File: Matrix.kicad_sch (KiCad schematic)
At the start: 56 parts

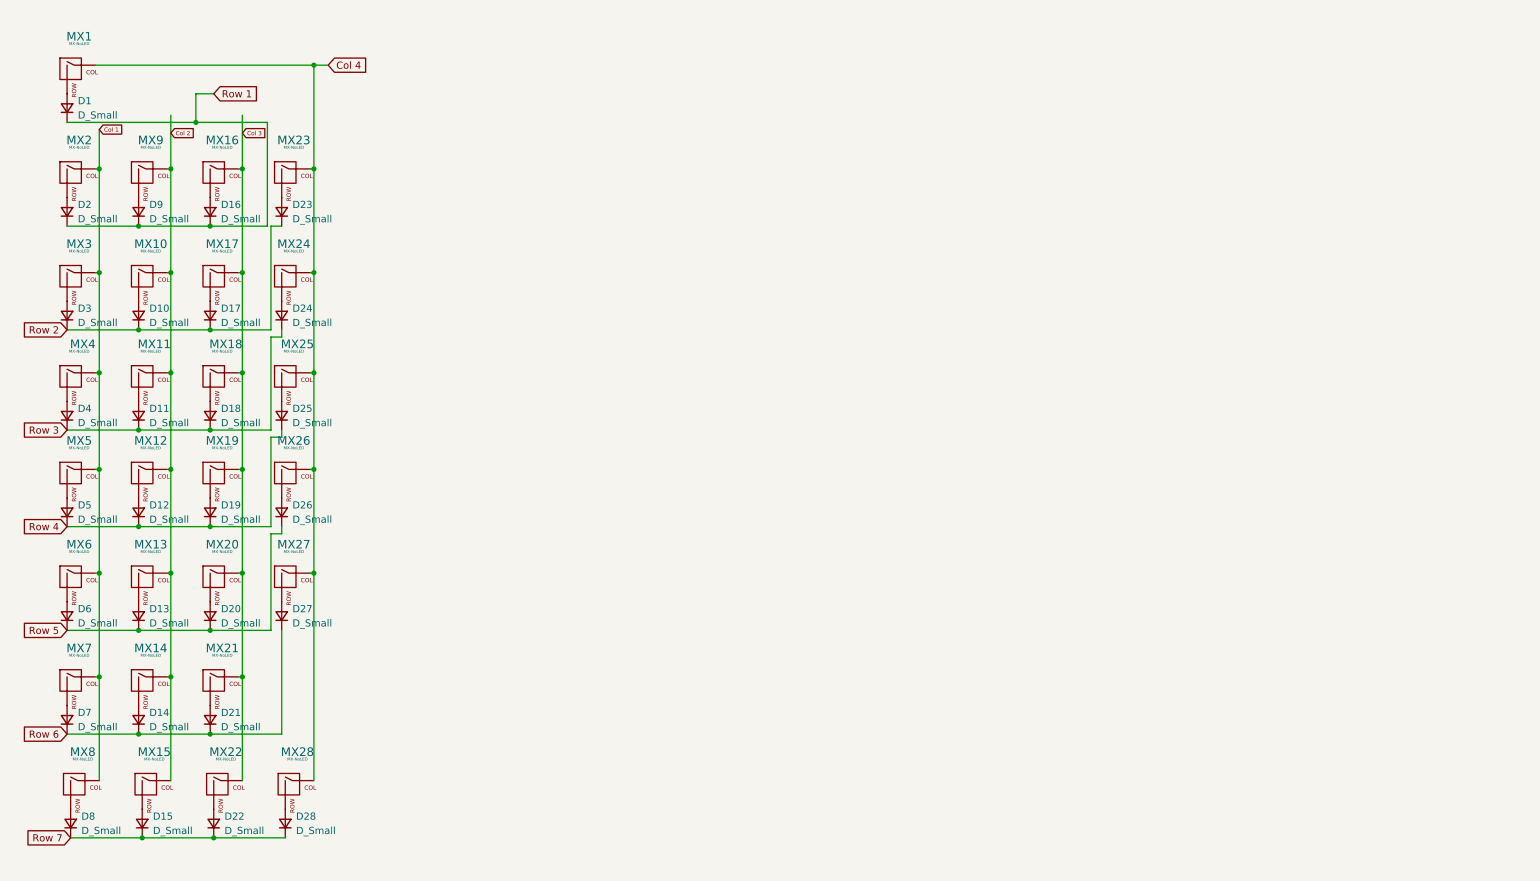
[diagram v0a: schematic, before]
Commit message: Schematic Finallized
Added ESD Protection to USB input and RGB LEDs
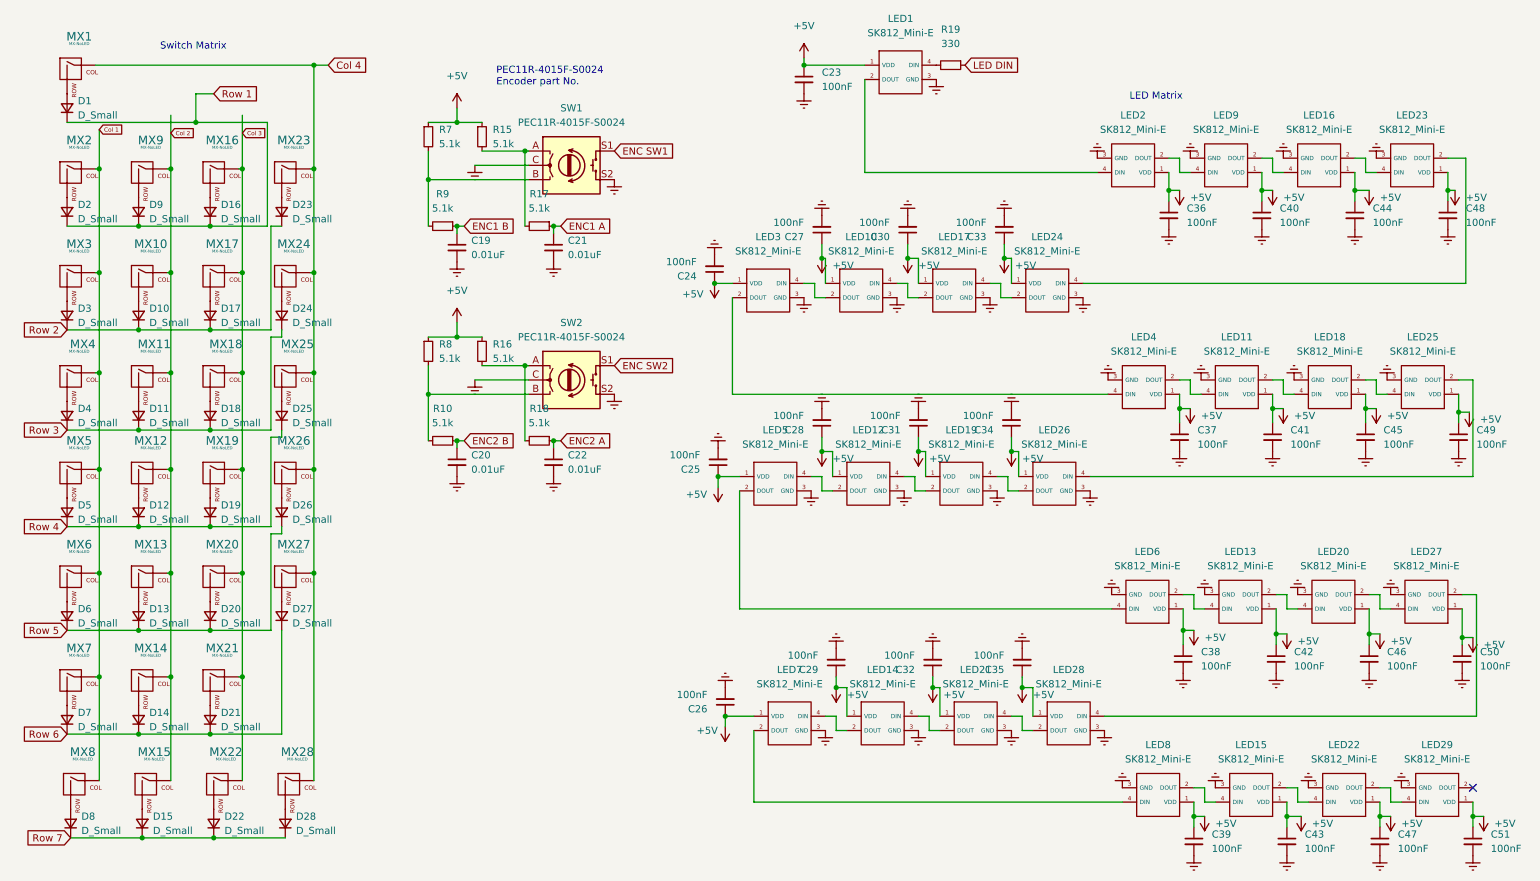
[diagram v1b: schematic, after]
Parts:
- added C19, C20, C21, C22: 0.01uF, Capacitor_SMD:C_0603_1608Metric_Pad1.08x0.95mm_HandSolder, symbol Device:C_Small
- added C23, C24, C25, C26, C27, C28, C29, C30, C31, C32, C33, C34, C35, C36, C37, C38, C39, C40, C41, C42, C43, C44, C45, C46, C47, C48, C49, C50, C51: 100nF, Capacitor_SMD:C_0603_1608Metric_Pad1.08x0.95mm_HandSolder, symbol Device:C_Small
- added LED1, LED10, LED11, LED12, LED13, LED14, LED15, LED16, LED17, LED18, LED19, LED2, LED20, LED21, LED22, LED23, LED24, LED25, LED26, LED27, LED28, LED29, LED3, LED4, LED5, LED6, LED7, LED8, LED9: SK812_Mini-E, Reset Switch:SK812 Mini-E, symbol Reset Switch:SK812_Mini-E
- added R10, R15, R16, R17, R18, R7, R8, R9: 5.1k, Resistor_SMD:R_0603_1608Metric_Pad0.98x0.95mm_HandSolder, symbol Device:R_Small
- added R19: 330, Resistor_SMD:R_0603_1608Metric_Pad0.98x0.95mm_HandSolder, symbol Device:R_Small
- added SW1, SW2: PEC11R-4015F-S0024, Reset Switch:PEC11R-4015F-S0024, symbol Reset Switch:PEC11R-4015F-S0024
- D1, D10, D11, D12, D13, D14, D15, D16, D17, D18, D19, D2, D20, D21, D22, D23, D24, D25, D26, D27, D28, D3, D4, D5, D6, D7, D8, D9: footprint (none) -> Diode_SMD:D_SOD-523
- MX1, MX10, MX11, MX12, MX13, MX14, MX15, MX16, MX17, MX18, MX19, MX2, MX20, MX21, MX22, MX23, MX24, MX25, MX26, MX27, MX3, MX4, MX5, MX6, MX7, MX8, MX9: footprint (none) -> MX_Only:MXOnly-1U-Hotswap
- MX28: footprint (none) -> MX_Only:MXOnly-2U-Hotswap-VerticalStabilizers
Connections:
- new net: R7.2, R9.2, SW1.B
- new net: LED18.2 (DOUT), LED25.4 (DIN)
- new net: LED11.2 (DOUT), LED18.4 (DIN)
- new net: LED22.2 (DOUT), LED29.4 (DIN)
- new net: R16.2, R18.2, SW2.A
- new net: R10.2, R8.2, SW2.B
- new net: LED27.2 (DOUT), LED28.4 (DIN)
- new net: LED20.2 (DOUT), LED27.4 (DIN)
- new net: LED14.4 (DIN), LED21.2 (DOUT)
- new net: LED21.4 (DIN), LED28.2 (DOUT)
- new net: LED13.2 (DOUT), LED20.4 (DIN)
- new net: LED13.4 (DIN), LED6.2 (DOUT)
- new net: LED25.2 (DOUT), LED26.4 (DIN)
- new net: LED5.2 (DOUT), LED6.4 (DIN)
- new net: LED16.2 (DOUT), LED23.4 (DIN)
- new net: LED16.4 (DIN), LED9.2 (DOUT)
- new net: R15.2, R17.2, SW1.A
- new net: LED1.4 (DIN), R19.2
- new net: LED10.2 (DOUT), LED3.4 (DIN)
- new net: LED10.4 (DIN), LED17.2 (DOUT)
- new net: LED19.4 (DIN), LED26.2 (DOUT)
- new net: LED23.2 (DOUT), LED24.4 (DIN)
- new net: LED12.2 (DOUT), LED5.4 (DIN)
- new net: LED12.4 (DIN), LED19.2 (DOUT)
- new net: LED17.4 (DIN), LED24.2 (DOUT)
- new net: LED3.2 (DOUT), LED4.4 (DIN)
- new net: LED15.2 (DOUT), LED22.4 (DIN)
- new net: LED15.4 (DIN), LED8.2 (DOUT)
- new net: LED7.2 (DOUT), LED8.4 (DIN)
- new net: LED14.2 (DOUT), LED7.4 (DIN)
- new net: LED2.2 (DOUT), LED9.4 (DIN)
- new net: LED1.2 (DOUT), LED2.4 (DIN)
- new net: LED11.4 (DIN), LED4.2 (DOUT)
- new net +5V: C23.1, C24.1, C25.1, C26.1, C27.1, C28.1, C29.1, C30.1, C31.1, C32.1, C33.1, C34.1, C35.1, C36.1, C37.1, C38.1, C39.1, C40.1, C41.1, C42.1, C43.1, C44.1, C45.1, C46.1, C47.1, C48.1, C49.1, C50.1, C51.1, LED1.1 (VDD), LED10.1 (VDD), LED11.1 (VDD), LED12.1 (VDD), LED13.1 (VDD), LED14.1 (VDD), LED15.1 (VDD), LED16.1 (VDD), LED17.1 (VDD), LED18.1 (VDD), LED19.1 (VDD), LED2.1 (VDD), LED20.1 (VDD), LED21.1 (VDD), LED22.1 (VDD), LED23.1 (VDD), LED24.1 (VDD), LED25.1 (VDD), LED26.1 (VDD), LED27.1 (VDD), LED28.1 (VDD), LED29.1 (VDD), LED3.1 (VDD), LED4.1 (VDD), LED5.1 (VDD), LED6.1 (VDD), LED7.1 (VDD), LED8.1 (VDD), LED9.1 (VDD), R15.1, R16.1, R7.1, R8.1
- new net ENC SW1: SW1.S1
- new net ENC SW2: SW2.S1
- new net ENC1 A: C21.1, R17.1
- new net ENC1 B: C19.1, R9.1
- new net ENC2 A: C22.1, R18.1
- new net ENC2 B: C20.1, R10.1
- new net Earth: C19.2, C20.2, C21.2, C22.2, C23.2, C24.2, C25.2, C26.2, C27.2, C28.2, C29.2, C30.2, C31.2, C32.2, C33.2, C34.2, C35.2, C36.2, C37.2, C38.2, C39.2, C40.2, C41.2, C42.2, C43.2, C44.2, C45.2, C46.2, C47.2, C48.2, C49.2, C50.2, C51.2, LED1.3 (GND), LED10.3 (GND), LED11.3 (GND), LED12.3 (GND), LED13.3 (GND), LED14.3 (GND), LED15.3 (GND), LED16.3 (GND), LED17.3 (GND), LED18.3 (GND), LED19.3 (GND), LED2.3 (GND), LED20.3 (GND), LED21.3 (GND), LED22.3 (GND), LED23.3 (GND), LED24.3 (GND), LED25.3 (GND), LED26.3 (GND), LED27.3 (GND), LED28.3 (GND), LED29.3 (GND), LED3.3 (GND), LED4.3 (GND), LED5.3 (GND), LED6.3 (GND), LED7.3 (GND), LED8.3 (GND), LED9.3 (GND), SW1.C, SW1.S2, SW2.C, SW2.S2
- new net LED DIN: R19.1
- no-connect marks 0 -> 1
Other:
- note added: "LED Matrix"
- note added: "PEC11R-4015F-S0024 Encoder part No."
- note added: "Switch Matrix"

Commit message: Layout Roughed in, routing started
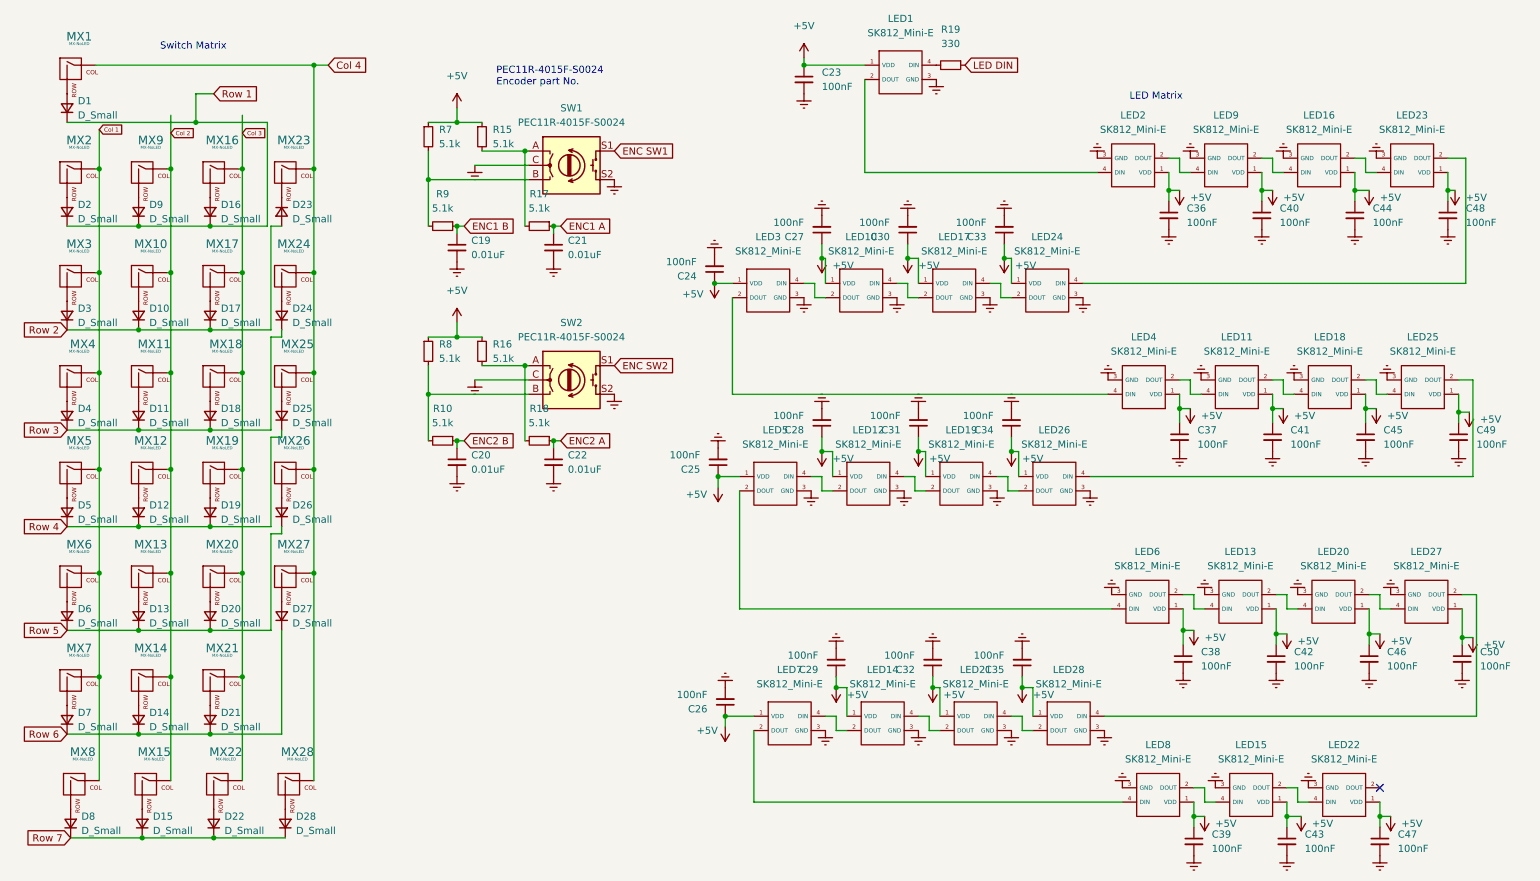
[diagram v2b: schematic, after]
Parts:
- removed C51: 100nF, Capacitor_SMD:C_0603_1608Metric_Pad1.08x0.95mm_HandSolder, symbol Device:C_Small
- removed LED29: SK812_Mini-E, Reset Switch:SK812 Mini-E, symbol Reset Switch:SK812_Mini-E
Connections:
- net Row 2: now also D23.2 (A); no longer D23.1 (K)
- net at MX23.2 (ROW): now also D23.1 (K); no longer D23.2 (A)
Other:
- moved on the sheet: D23
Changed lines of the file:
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@@
   (junction (at 68.58 76.2) (diameter 0) (color 0 0 0 0)
   )
-  (junction (at 274.32 154.94) (diameter 0) (color 0 0 0 0)
-  )
   (junction (at 50.165 68.58) (diameter 0) (color 0 0 0 0)
   )
@@
   (junction (at 55.88 111.76) (diameter 0) (color 0 0 0 0)
   )
-  (no_connect (at 274.32 149.86))
+  (no_connect (at 257.81 149.86))
   (wire (pts (xy 158.75 53.34) (xy 158.75 55.88))
     (stroke (width 0) (type default) (color 0 0 0 0))
@@
     (stroke (width 0) (type default) (color 0 0 0 0))
   )
-  (wire (pts (xy 257.81 149.86) (xy 259.715 149.86))
-    (stroke (width 0) (type default) (color 0 0 0 0))
-  )
   (wire (pts (xy 224.79 152.4) (xy 224.79 154.94))
     (stroke (width 0) (type default) (color 0 0 0 0))
@@
     (stroke (width 0) (type default) (color 0 0 0 0))
   )
-  (wire (pts (xy 259.715 149.86) (xy 259.715 152.4))
-    (stroke (width 0) (type default) (color 0 0 0 0))
-  )
   (wire (pts (xy 37.465 121.92) (xy 50.165 121.92))
     (stroke (width 0) (type default) (color 0 0 0 0))
@@
     (stroke (width 0) (type default) (color 0 0 0 0))
   )
+  (wire (pts (xy 60.325 31.75) (xy 60.325 50.165))
+    (stroke (width 0) (type default) (color 0 0 0 0))
+  )
   (wire (pts (xy 60.96 103.505) (xy 60.96 87.63))
     (stroke (width 0) (type default) (color 0 0 0 0))
@@
     (stroke (width 0) (type default) (color 0 0 0 0))
   )
-  (wire (pts (xy 274.32 154.94) (xy 274.32 156.845))
-    (stroke (width 0) (type default) (color 0 0 0 0))
-  )
-  (wire (pts (xy 60.325 50.165) (xy 60.325 31.75))
-    (stroke (width 0) (type default) (color 0 0 0 0))
-  )
   (wire (pts (xy 50.8 158.75) (xy 63.5 158.75))
     (stroke (width 0) (type default) (color 0 0 0 0))
@@
     (stroke (width 0) (type default) (color 0 0 0 0))
   )
-  (wire (pts (xy 259.715 152.4) (xy 261.62 152.4))
-    (stroke (width 0) (type default) (color 0 0 0 0))
-  )
   (wire (pts (xy 255.27 82.55) (xy 255.27 85.09))
     (stroke (width 0) (type default) (color 0 0 0 0))
@@
     (stroke (width 0) (type default) (color 0 0 0 0))
   )
-  (wire (pts (xy 274.32 154.94) (xy 276.225 154.94))
-    (stroke (width 0) (type default) (color 0 0 0 0))
-  )
   (wire (pts (xy 67.945 76.2) (xy 68.58 76.2))
     (stroke (width 0) (type default) (color 0 0 0 0))
@@
     (stroke (width 0) (type default) (color 0 0 0 0))
   )
-  (wire (pts (xy 274.32 152.4) (xy 274.32 154.94))
-    (stroke (width 0) (type default) (color 0 0 0 0))
-  )
   (wire (pts (xy 241.3 152.4) (xy 241.3 154.94))
     (stroke (width 0) (type default) (color 0 0 0 0))
@@
     (pin "2")
   )
-  (symbol (lib_id "power:+5V") (at 276.225 154.94 180) (unit 1)
-    (in_bom yes) (on_board yes) (fields_autoplaced)
-    (property "Reference" "#PWR0138" (id 0) (at 276.225 151.13 0)
-      (effects (font (size 1.27 1.27)) hide)
-    )
-    (property "Value" "+5V" (id 1) (at 278.13 156.2099 0)
-      (effects (font (size 1.27 1.27)) (justify right))
-    )
-    (property "Footprint" "" (id 2) (at 276.225 154.94 0)
-      (effects (font (size 1.27 1.27)) hide)
-    )
-    (property "Datasheet" "" (id 3) (at 276.225 154.94 0)
-      (effects (font (size 1.27 1.27)) hide)
-    )
-    (pin "1")
-  )
   (symbol (lib_id "power:Earth") (at 159.385 139.7 0) (unit 1)
     (in_bom yes) (on_board yes) (fields_autoplaced)
@@
     (pin "2")
   )
-  (symbol (lib_id "Device:C_Small") (at 274.32 159.385 0) (unit 1)
-    (in_bom yes) (on_board yes) (fields_autoplaced)
-    (property "Reference" "C51" (id 0) (at 277.495 158.1212 0)
-      (effects (font (size 1.27 1.27)) (justify left))
-    )
-    (property "Value" "100nF" (id 1) (at 277.495 160.6612 0)
-      (effects (font (size 1.27 1.27)) (justify left))
-    )
-    (property "Footprint" "Capacitor_SMD:C_0603_1608Metric_Pad1.08x0.95mm_HandSolder" (id 2) (at 274.32 159.385 0)
-      (effects (font (size 1.27 1.27)) hide)
-    )
-    (property "Datasheet" "~" (id 3) (at 274.32 159.385 0)
-      (effects (font (size 1.27 1.27)) hide)
-    )
-    (pin "1")
-    (pin "2")
-  )
   (symbol (lib_id "MX_Alps_Hybrid:MX-NoLED") (at 64.135 77.47 0) (unit 1)
     (in_bom yes) (on_board yes)
@@
     (pin "4")
   )
-  (symbol (lib_id "Reset Switch:SK812_Mini-E") (at 271.78 154.94 180) (unit 1)
-    (in_bom yes) (on_board yes) (fields_autoplaced)
-    (property "Reference" "LED29" (id 0) (at 267.97 142.24 0))
-    (property "Value" "SK812_Mini-E" (id 1) (at 267.97 144.78 0))
-    (property "Footprint" "Reset Switch:SK812 Mini-E" (id 2) (at 270.51 158.75 0)
-      (effects (font (size 1.27 1.27)) hide)
-    )
-    (property "Datasheet" "" (id 3) (at 270.51 158.75 0)
-      (effects (font (size 1.27 1.27)) hide)
-    )
-    (pin "1")
-    (pin "2")
-    (pin "3")
-    (pin "4")
-  )
-  (symbol (lib_id "power:Earth") (at 261.62 149.86 180) (unit 1)
-    (in_bom yes) (on_board yes) (fields_autoplaced)
-    (property "Reference" "#PWR0130" (id 0) (at 261.62 143.51 0)
-      (effects (font (size 1.27 1.27)) hide)
-    )
-    (property "Value" "Earth" (id 1) (at 261.62 146.05 0)
-      (effects (font (size 1.27 1.27)) hide)
-    )
-    (property "Footprint" "" (id 2) (at 261.62 149.86 0)
-      (effects (font (size 1.27 1.27)) hide)
-    )
-    (property "Datasheet" "~" (id 3) (at 261.62 149.86 0)
-      (effects (font (size 1.27 1.27)) hide)
-    )
-    (pin "1")
-  )
   (symbol (lib_id "Device:D_Small") (at 50.165 100.965 90) (unit 1)
     (in_bom yes) (on_board yes) (fields_autoplaced)
@@
     (pin "1")
   )
-  (symbol (lib_id "power:Earth") (at 274.32 161.925 0) (unit 1)
-    (in_bom yes) (on_board yes) (fields_autoplaced)
-    (property "Reference" "#PWR0137" (id 0) (at 274.32 168.275 0)
-      (effects (font (size 1.27 1.27)) hide)
-    )
-    (property "Value" "Earth" (id 1) (at 274.32 165.735 0)
-      (effects (font (size 1.27 1.27)) hide)
-    )
-    (property "Footprint" "" (id 2) (at 274.32 161.925 0)
-      (effects (font (size 1.27 1.27)) hide)
-    )
-    (property "Datasheet" "~" (id 3) (at 274.32 161.925 0)
-      (effects (font (size 1.27 1.27)) hide)
-    )
-    (pin "1")
-  )
   (symbol (lib_id "Device:C_Small") (at 239.395 127 0) (unit 1)
     (in_bom yes) (on_board yes) (fields_autoplaced)
@@
     (pin "2")
   )
-  (symbol (lib_id "Device:D_Small") (at 62.865 47.625 90) (unit 1)
+  (symbol (lib_id "Device:D_Small") (at 62.865 47.625 270) (unit 1)
     (in_bom yes) (on_board yes) (fields_autoplaced)
     (property "Reference" "D23" (id 0) (at 64.77 46.3549 90)
-      (effects (font (size 1.27 1.27)) (justify right))
+      (effects (font (size 1.27 1.27)) (justify left))
     )
     (property "Value" "D_Small" (id 1) (at 64.77 48.8949 90)
-      (effects (font (size 1.27 1.27)) (justify right))
+      (effects (font (size 1.27 1.27)) (justify left))
     )
     (property "Footprint" "Diode_SMD:D_SOD-523" (id 2) (at 62.865 47.625 90)
